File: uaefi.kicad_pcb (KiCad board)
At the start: 4 copper layers, 100 x 100 mm, 159 parts, among them J1 Conn_02x02_Odd_Even, J10 5569-16A2, J11 Conn_02x02_Odd_Even, J12 Conn_02x02_Odd_Even, J13 Conn_02x02_Odd_Even, J14 Conn_02x02_Odd_Even, J15 Conn_02x02_Odd_Even, J16 Conn_02x02_Odd_Even, J17 Conn_02x02_Odd_Even, J18 Conn_02x02_Odd_Even, J19 Conn_02x02_Odd_Even, J2 5569-20A2, J20 Conn_02x02_Odd_Even, J21 Conn_02x02_Odd_Even, J22 Conn_02x02_Odd_Even, J24 Conn_02x02_Odd_Even, J3 5569-06A2, J4 5569-08A2, J5 5569-18A2, J6 Conn_01x06, J7 Conn_01x05_Male, J8 USB_B_Mini, J9 USB_C, M1 Module-power_12and5V-0.3, M2 Module-knock-0.2, M3 Module-vr-discrete-0.5, M4 Module-vr-max9924-0.1, M5 Module-wbo-0.5, M6 Module:mega-mcu100/0.3, M7 Module-can-0.1, P1 Pad, P15 Pad, P16 Pad, P17 Pad, P18 Pad, P2 Pad, P3 Pad, P4 Pad, P5 Pad, P6 Pad, P7 Pad, P8 Pad, Q10 ISL9V3040D3ST, Q11 ISL9V3040D3ST, Q12 ISL9V3040D3ST, Q7 ISL9V3040D3ST, Q8 ISL9V3040D3ST, Q9 ISL9V3040D3ST, U1 TLE9201SG, U10 VNLD5160TR-E, U11 VNLD5160TR-E, U2 TLE9201SG, U3 MPX4/MPXH6400_MAP, U4 MAX31855KASA, U5 JDY-33, U6 VNLD5160TR-E, U7 VNLD5160TR-E, U8 VNLD5160TR-E, U9 VNLD5160TR-E

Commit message: Replace Mini-Fit harness connectors with two AMPSEAL 35 headers.
Map rev E loom nets onto J30 and J31, document the pinout, and place unverified 776163-1 footprints without re-routing.

Co-authored-by: Quintin <quintinbannink42@users.noreply.github.com>
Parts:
- removed J10: 5569-16A2, Connector_Molex:Molex_Mini-Fit_Jr_5569-16A2_2x08_P4.20mm_Horizontal
- removed J2: 5569-20A2, Connector_Molex:Molex_Mini-Fit_Jr_5569-20A2_2x10_P4.20mm_Horizontal
- removed J3: 5569-06A2, Connector_Molex:Molex_Mini-Fit_Jr_5569-06A2_2x03_P4.20mm_Horizontal
- removed J4: 5569-08A2, Connector_Molex:Molex_Mini-Fit_Jr_5569-08A2_2x04_P4.20mm_Horizontal
- removed J5: 5569-18A2, Connector_Molex:Molex_Mini-Fit_Jr_5569-18A2_2x09_P4.20mm_Horizontal
- added J30: 776163-1, ampseal:TE_AMPSEAL_35_776163-1, F.Cu at (62.0, 148.0)
- added J31: 776163-1, ampseal:TE_AMPSEAL_35_776163-1, F.Cu at (140.0, 148.0)

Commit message: Fit both AMPSEAL headers on edge tabs and drop dead Mini-Fit tracks.
Add a bottom tab for J30 and a right tab for J31, hang the right-angle bodies off the outline, and remove segments that ended on the old harness pads.

Co-authored-by: Quintin <quintinbannink42@users.noreply.github.com>
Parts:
- moved J31 32.2 mm to (168.0, 132.0), turned to 90 degrees
- moved J30 19.1 mm to (68.4, 166.0)
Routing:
- net GNDA: track 155.8 -> 136.0 mm
- net +5VP: track 199.7 -> 180.1 mm
- net /IN_BUTTON2: track 76.2 -> 65.1 mm
- net /WBO_Rtrim: track 10.8 -> 2.19 mm
- net /IN_AUX2: track 85.1 -> 78.2 mm
- net /IN_BUTTON1: track 81.9 -> 75.7 mm
- net /EGT+: track 10.1 -> 4.17 mm
- net /VR_DISCRETE+: track 9.83 -> 4.01 mm
- net +12V: track 25.7 -> 20.3 mm
- net /IN_PPS2: track 78.2 -> 72.9 mm
- net /OUT_IGN5: track 29.6 -> 24.4 mm
- net /OUT_LS4: track 11.3 -> 6.95 mm
- net /IN_HALL1: track 70.3 -> 66.2 mm
- net /OUT_DC1+: track 17.1 -> 13.1 mm
- net /12V_KEY: track 19.3 -> 15.5 mm
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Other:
- board size 100 x 100 mm -> 130 x 118 mm
- board text added: "AMPSEAL tabs: J30 bottom, J31 right. Bodies hang off the outline. Footprint unverified."

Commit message: Seat the AMPSEAL headers on opposite edges of a taller rectangle.
Drop the right-side tab, keep J30 on the bottom, and move J31 to the top so the outline stays a rounded Hellen-One-style carrier.

Co-authored-by: Quintin <quintinbannink42@users.noreply.github.com>
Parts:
- moved J31 95.0 mm to (112.4, 55.0), turned to 180 degrees
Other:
- board size 130 x 118 mm -> 100 x 136 mm
- board text added: "J30 bottom, J31 top. Shells hang off the outline. Same family as uaEFI, not a clone. Footprint unverified."
- board text removed: "AMPSEAL tabs: J30 bottom, J31 right. Bodies hang off the outline. Footprint unverified."
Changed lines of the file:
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@@
 	(footprint "ampseal:TE_AMPSEAL_35_776163-1"
 		(layer "F.Cu")
-		(at 168 132 90)
+		(at 112.4 55 180)
 		(descr "TE AMPSEAL 35-pin header 776163-1 family. Footprint hypothesis; see docs/ampseal-35-pinout.md")
 		(property "Reference" "J31"
@@
 		)
 	)
+	(gr_arc
+		(start 50 45.5)
+		(mid 51.025126 43.025126)
+		(end 53.5 42)
+		(stroke
+			(width 0.1)
+			(type default)
+		)
+		(layer "Edge.Cuts")
+	)
 	(gr_line
-		(start 96.5 106.2)
-		(end 102.9 106.2)
-		(stroke
-			(width 0.15)
-			(type default)
-		)
-		(layer "F.SilkS")
+		(start 53.5 42)
+		(end 146.5 42)
+		(stroke
+			(width 0.1)
+			(type default)
+		)
+		(layer "Edge.Cuts")
+	)
+	(gr_arc
+		(start 146.5 42)
+		(mid 148.974874 43.025126)
+		(end 150 45.5)
+		(stroke
+			(width 0.1)
+			(type default)
+		)
+		(layer "Edge.Cuts")
 	)
 	(gr_line
-		(start 96.5 108.8)
-		(end 102.9 108.8)
-		(stroke
-			(width 0.15)
-			(type default)
-		)
-		(layer "F.SilkS")
+		(start 150 45.5)
+		(end 150 174.5)
+		(stroke
+			(width 0.1)
+			(type default)
+		)
+		(layer "Edge.Cuts")
+	)
+	(gr_arc
+		(start 150 174.5)
+		(mid 148.974874 176.974874)
+		(end 146.5 178)
+		(stroke
+			(width 0.1)
+			(type default)
+		)
+		(layer "Edge.Cuts")
 	)
 	(gr_line
-		(start 88.8 101.2)
-		(end 95.2 101.2)
-		(stroke
-			(width 0.15)
-			(type default)
-		)
-		(layer "F.SilkS")
-	)
-	(gr_rect
-		(start 79.27 130.067565)
-		(end 92.186015 137.642435)
-		(stroke
-			(width 0.15)
-			(type solid)
-		)
-		(fill solid)
-		(layer "F.SilkS")
+		(start 146.5 178)
+		(end 53.5 178)
+		(stroke
+			(width 0.1)
+			(type default)
+		)
+		(layer "Edge.Cuts")
+	)
+	(gr_arc
+		(start 53.5 178)
+		(mid 51.025126 176.974874)
+		(end 50 174.5)
+		(stroke
+			(width 0.1)
+			(type default)
+		)
+		(layer "Edge.Cuts")
 	)
 	(gr_line
-		(start 96.5 103.8)
-		(end 102.9 103.8)
-		(stroke
-			(width 0.15)
-			(type default)
-		)
-		(layer "F.SilkS")
-	)
-	(gr_line
-		(start 88.8 106.2)
-		(end 95.2 106.2)
-		(stroke
-			(width 0.15)
-			(type default)
-		)
-		(layer "F.SilkS")
-	)
-	(gr_line
-		(start 96.5 101.2)
-		(end 102.9 101.2)
-		(stroke
-			(width 0.15)
-			(type default)
-		)
-		(layer "F.SilkS")
-	)
-	(gr_line
-		(start 88.8 103.8)
-		(end 95.2 103.8)
-		(stroke
-			(width 0.15)
-			(type default)
-		)
-		(layer "F.SilkS")
-	)
-	(gr_arc
-		(start 50 63.5)
-		(mid 51.025126 61.025126)
-		(end 53.5 60)
-		(stroke
-			(width 0.1)
-			(type default)
-		)
-		(layer "Edge.Cuts")
-	)
-	(gr_arc
-		(start 150 156.5)
-		(mid 148.974874 158.974874)
-		(end 146.5 160)
-		(stroke
-			(width 0.1)
-			(type default)
-		)
-		(layer "Edge.Cuts")
-	)
-	(gr_line
-		(start 150 156.5)
-		(end 150 150)
-		(stroke
-			(width 0.1)
-			(type default)
-		)
-		(layer "Edge.Cuts")
-	)
-	(gr_line
-		(start 150 150)
-		(end 180 150)
-		(stroke
-			(width 0.1)
-			(type default)
-		)
-		(layer "Edge.Cuts")
-	)
-	(gr_line
-		(start 180 150)
-		(end 180 70)
-		(stroke
-			(width 0.1)
-			(type default)
-		)
-		(layer "Edge.Cuts")
-	)
-	(gr_line
-		(start 180 70)
-		(end 150 70)
-		(stroke
-			(width 0.1)
-			(type default)
-		)
-		(layer "Edge.Cuts")
-	)
-	(gr_line
-		(start 150 70)
-		(end 150 63.5)
-		(stroke
-			(width 0.1)
-			(type default)
-		)
-		(layer "Edge.Cuts")
-	)
-	(gr_text "AMPSEAL tabs: J30 bottom, J31 right. Bodies hang off the outline. Footprint unverified."
-		(at 100 64 0)
+		(start 50 174.5)
+		(end 50 45.5)
+		(stroke
+			(width 0.1)
+			(type default)
+		)
+		(layer "Edge.Cuts")
+	)
+	(gr_text "J30 bottom, J31 top. Shells hang off the outline. Same family as uaEFI, not a clone. Footprint unverified."
+		(at 100 66 0)
 		(layer "Cmts.User")
-		(effects (font (size 1.2 1.2) (thickness 0.15)))
-	)
-	(gr_line
-		(start 50 63.5)
-		(end 50 156.5)
-		(stroke
-			(width 0.1)
-			(type default)
-		)
-		(layer "Edge.Cuts")
-	)
-	(gr_line
-		(start 146.5 60)
-		(end 53.5 60)
-		(stroke
-			(width 0.1)
-			(type default)
-		)
-		(layer "Edge.Cuts")
-	)
-	(gr_arc
-		(start 53.5 160)
-		(mid 51.025126 158.974874)
-		(end 50 156.5)
-		(stroke
-			(width 0.1)
-			(type default)
-		)
-		(layer "Edge.Cuts")
-	)
-	(gr_arc
-		(start 146.5 60)
-		(mid 148.974874 61.025126)
-		(end 150 63.5)
-		(stroke
-			(width 0.1)
-			(type default)
-		)
-		(layer "Edge.Cuts")
-	)
-	(gr_line
-		(start 53.5 160)
-		(end 58 160)
-		(stroke
-			(width 0.1)
-			(type default)
-		)
-		(layer "Edge.Cuts")
-	)
-	(gr_line
-		(start 58 160)
-		(end 58 178)
-		(stroke
-			(width 0.1)
-			(type default)
-		)
-		(layer "Edge.Cuts")
-	)
-	(gr_line
-		(start 58 178)
-		(end 124 178)
-		(stroke
-			(width 0.1)
-			(type default)
-		)
-		(layer "Edge.Cuts")
-	)
-	(gr_line
-		(start 124 178)
-		(end 124 160)
-		(stroke
-			(width 0.1)
-			(type default)
-		)
-		(layer "Edge.Cuts")
-	)
-	(gr_line
-		(start 124 160)
-		(end 146.5 160)
-		(stroke
-			(width 0.1)
-			(type default)
-		)
-		(layer "Edge.Cuts")
+		(effects (font (size 1.1 1.1) (thickness 0.15)))
 	)
 	(gr_text "GND"

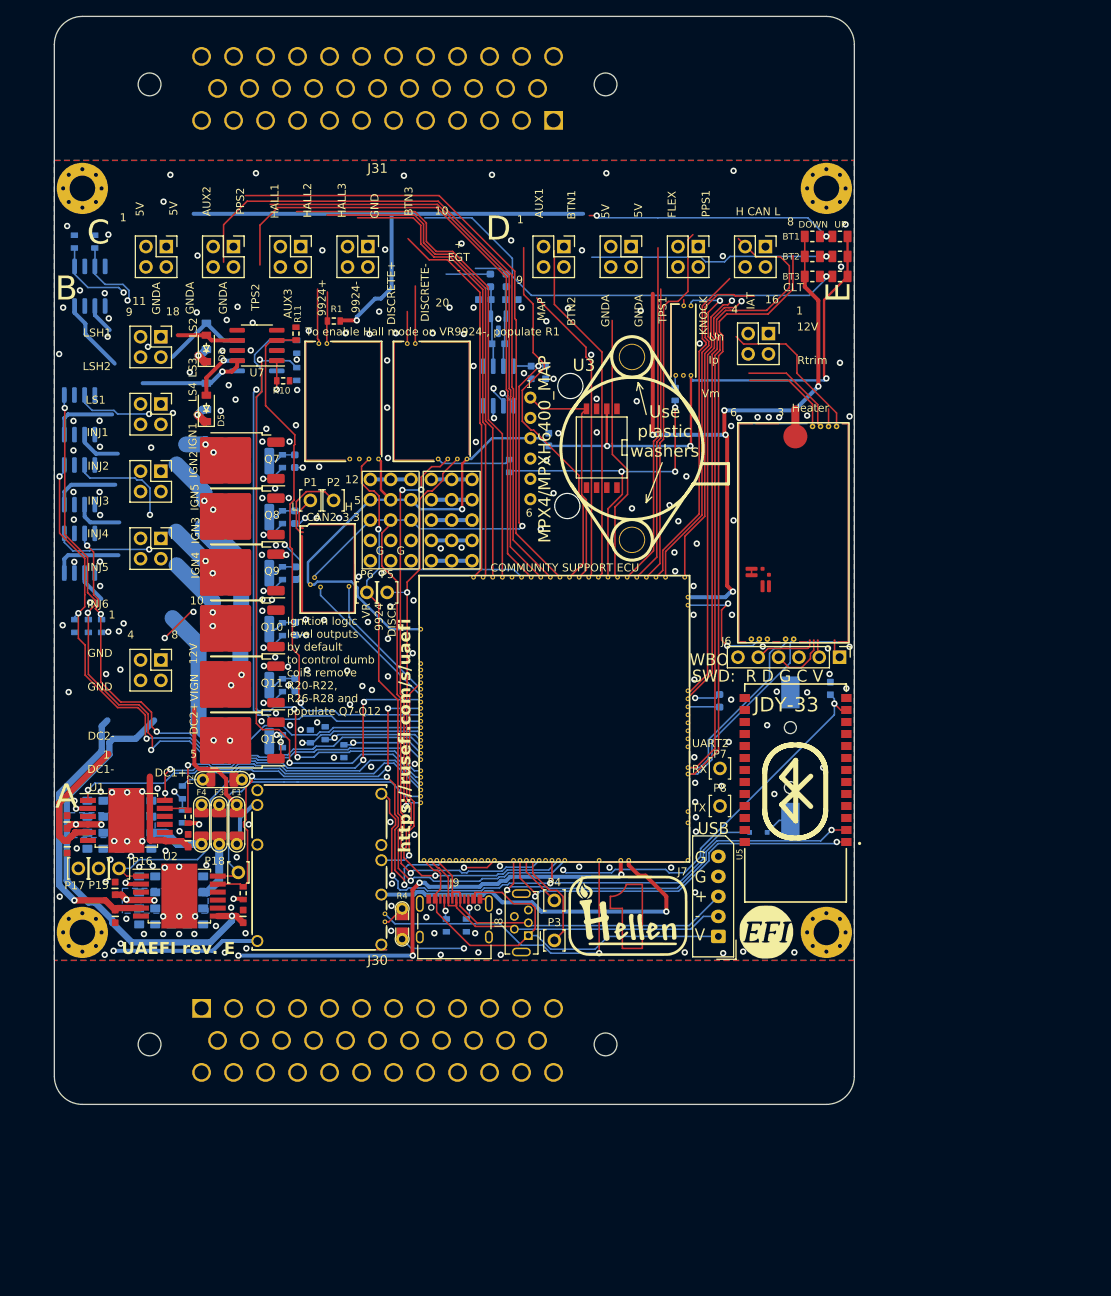
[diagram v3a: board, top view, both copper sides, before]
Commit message: Remove dumb-coil IGBTs and route the AMPSEAL header pins.
Drop Q7-Q12 from the ignition sheet and the board, track every J30/J31 signal pad to existing copper, and document the remaining KiCad 8 fab steps.

Co-authored-by: Quintin <quintinbannink42@users.noreply.github.com>
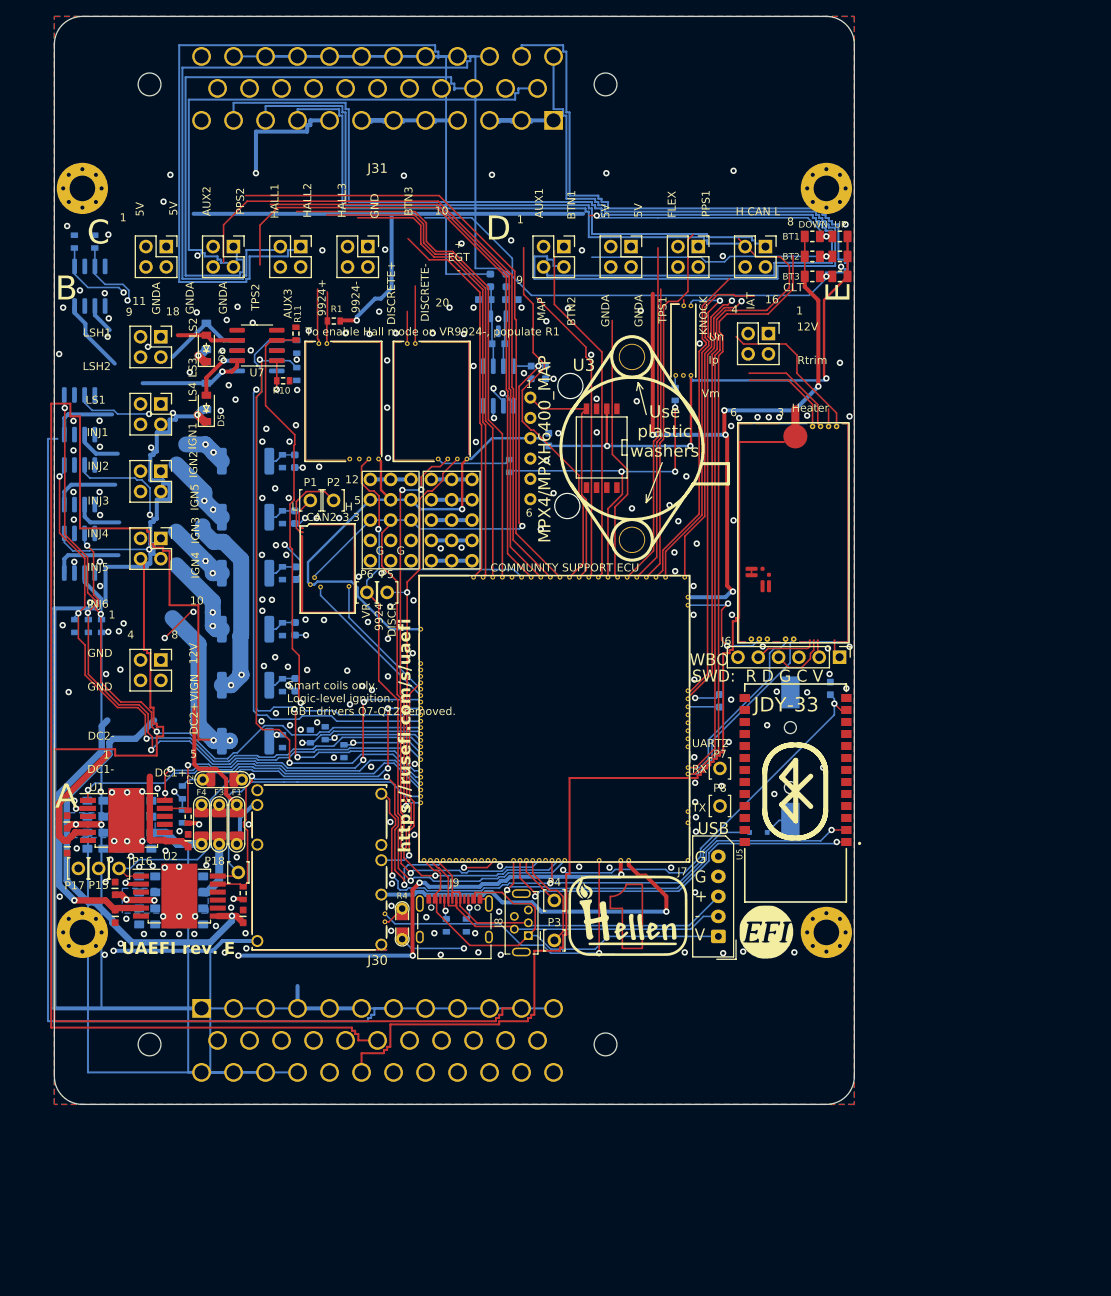
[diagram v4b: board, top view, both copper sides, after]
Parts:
- removed Q10, Q11, Q12, Q7, Q8, Q9: ISL9V3040D3ST, Package_TO_SOT_SMD:TO-252-2
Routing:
- net /WBO_Rtrim: track 2.19 -> 284.2 mm
- net /OUT_LS1: track 13.4 -> 227.8 mm
- net /OUT_LS4: track 6.95 -> 211.3 mm
- net /VR_DISCRETE+: track 4.01 -> 201.0 mm
- net /OUT_LS2: track 7.69 -> 190.5 mm
- net /OUT_IGN6: track 19.5 -> 201.9 mm
- net /VR_MAX9924-: track 6.49 -> 179.9 mm
- net /VR_MAX9924+: track 6.89 -> 167.5 mm
- net /VR_DISCRETE-: track 7.21 -> 150.2 mm
- net /WBO_Ip: track 13.1 -> 155.1 mm
- net /WBO_Vm: track 11.9 -> 150.3 mm
- net /WBO_Un: track 19.5 -> 156.3 mm
- net /OUT_LS_HOT1: track 3.77 -> 140.2 mm
- net /OUT_INJ5: track 8.74 -> 143.5 mm
- net /IN_MAP: track 37.9 -> 172.5 mm
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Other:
- board text added: "Smart coils only. Logic-level ignition. IGBT drivers Q7-Q12 removed."
- board text removed: "Ignition logic level outputs by default to control dumb coils remove R20-R22, R26-R28 and populate Q7-Q12"
